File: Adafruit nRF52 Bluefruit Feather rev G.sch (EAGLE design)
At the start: 49 parts, among them Q3 DMG3415U-7, SW1 KMR2, SW2 KMR2, U1 MDBT42, U2 AP2112(3.3V), U3 MCP73831T-2ACI/OT, U4 CP2104, X1 4u20317, X2 JSTPH, X3 4u20329, X4 32.768

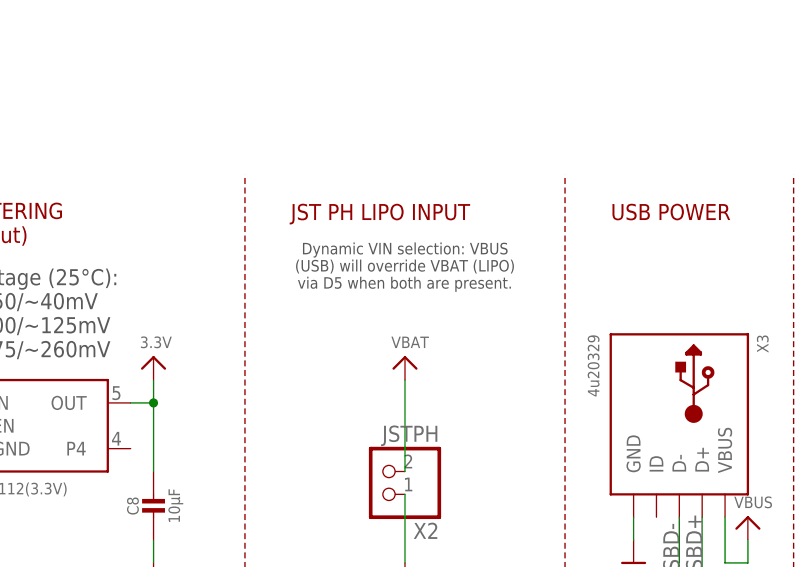
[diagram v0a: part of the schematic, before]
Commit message: Fixing typo: D5 -> D1
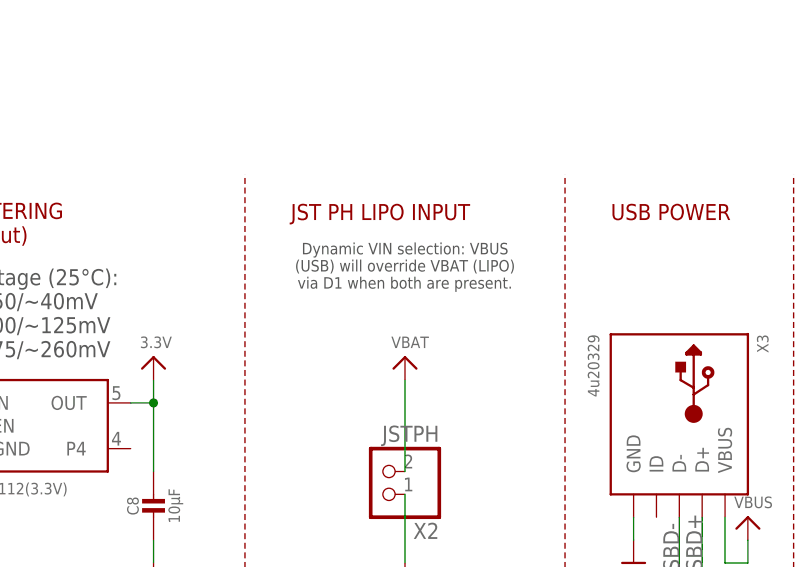
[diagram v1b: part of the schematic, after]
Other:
- note added: "Dynamic VIN selection: VBUS (USB) will override VBAT (LIPO) via D1 when both are present."
- note removed: "Dynamic VIN selection: VBUS (USB) will override VBAT (LIPO) via D5 when both are present."
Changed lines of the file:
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@@
 <text x="93.98" y="165.1" size="1.27" layer="97" align="center">Dynamic VIN selection: VBUS
 (USB) will override VBAT (LIPO)
-via D5 when both are present.</text>
+via D1 when both are present.</text>
 <text x="35.56" y="154.94" size="1.778" layer="97">Dropout Voltage (25°C):
 100mA: ~250/~40mV
